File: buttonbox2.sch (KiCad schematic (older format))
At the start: 58 parts, among them J2 AVR-PDI-6, J4 Conn_01x03_Male, SW1 SW_SP3T, SW10 SW_Push, SW11 SW_Push, SW12 SW_Push, SW13 SW_Push, SW14 SW_Push, SW15 SW_Push, SW16 SW_Push, SW17 SW_Push, SW18 SW_Push, SW19 SW_Push, SW20 SW_Push, SW21 SW_Push, SW22 SW_Push, SW23 SW_Push, SW24 SW_Push, SW25 SW_Push, SW26 SW_Push, SW27 SW_Push, SW28 SW_Push, SW29 SW_Push, SW30 SW_Push, SW31 SW_Push, SW32 SW_Push, SW33 SW_Push, SW34 SW_Push, SW35 SW_Push, SW36 SW_Push, SW37 SW_Push, SW38 SW_Push, SW39 SW_Push, SW40 SW_Push, SW5 SW_Push, SW6 SW_Push, SW7 SW_Push, SW8 SW_Push, SW9 SW_Push, U1 ATxmega256A3-AU, U6 AMS1117-3.3, Y2 Crystal_GND24

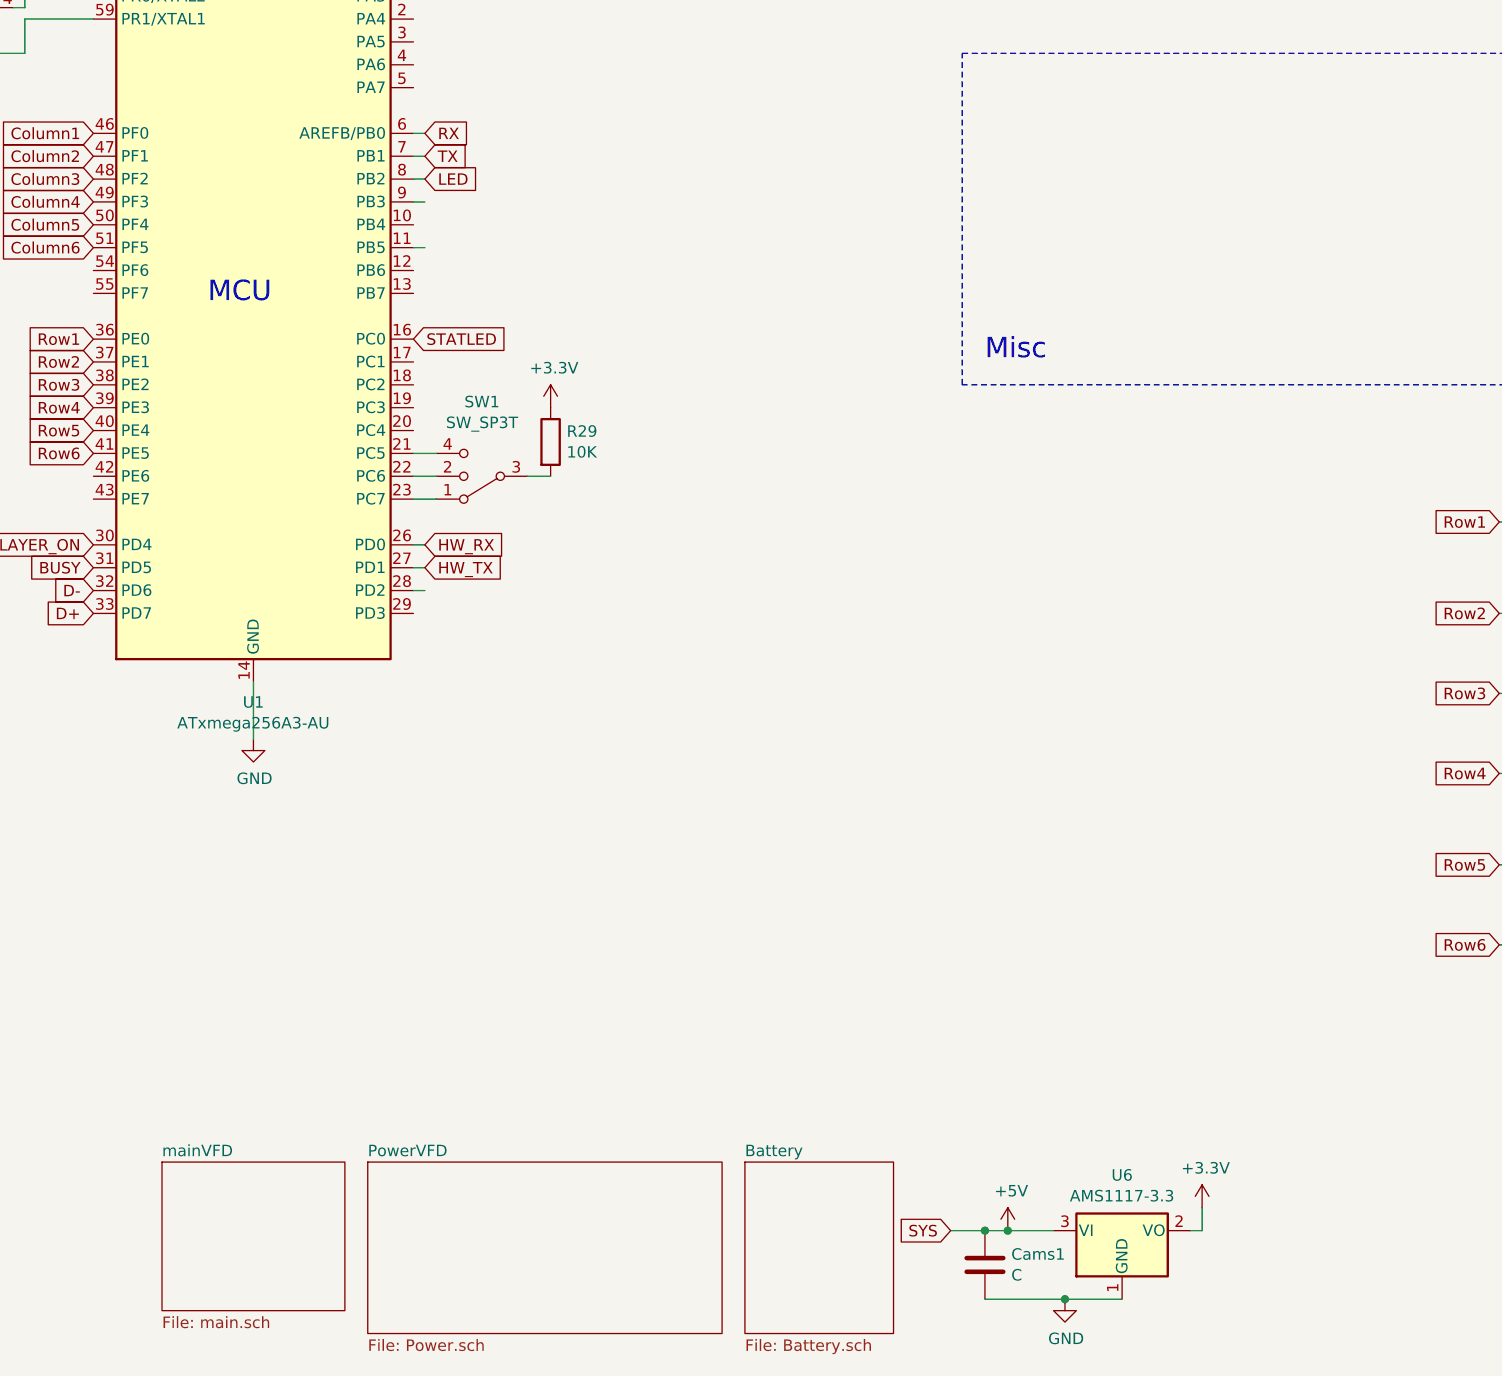
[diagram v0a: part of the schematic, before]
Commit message: Added hardware battery disconnect
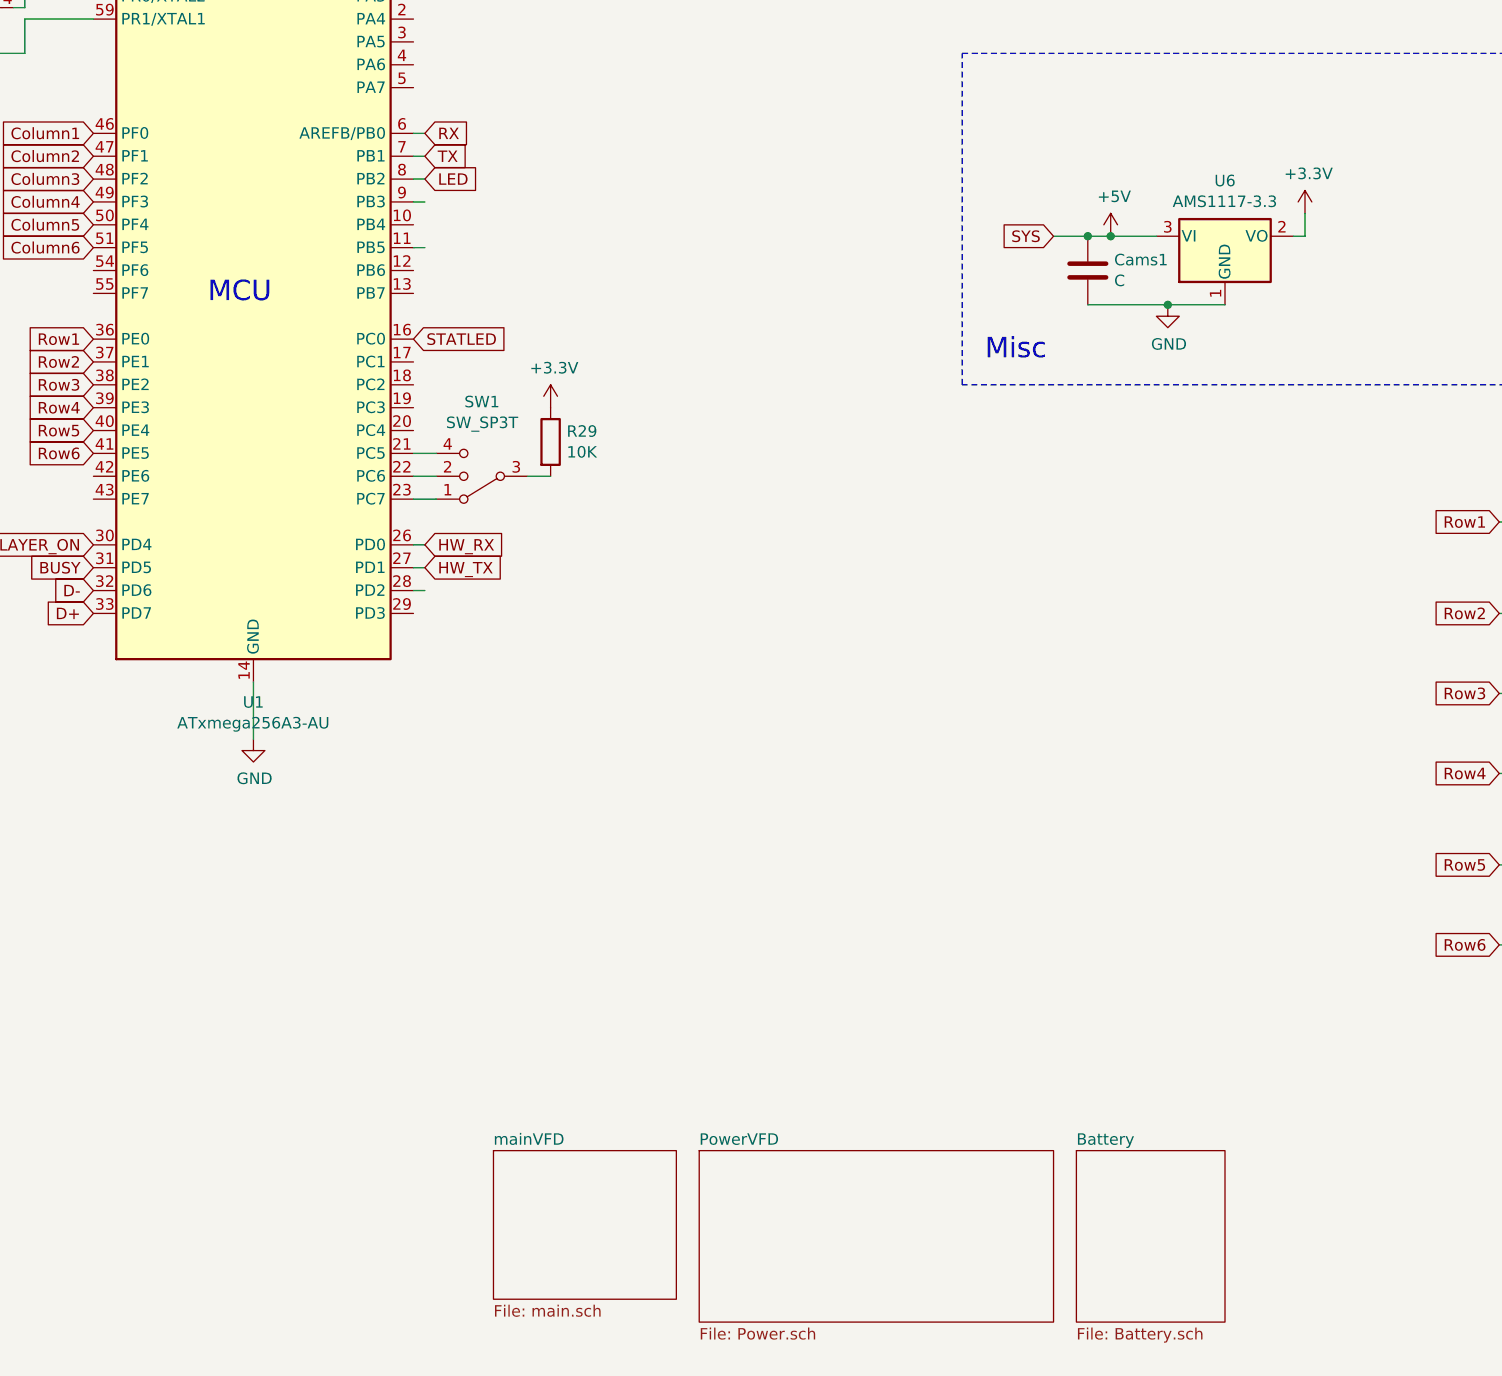
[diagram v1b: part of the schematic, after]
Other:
- moved on the sheet: Cams1, U6
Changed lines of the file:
@@
 L power:+3.3V #PWR0101
 U 1 1 617F15D4
-P 6750 7150
-F 0 "#PWR0101" H 6750 7000 50  0001 C CNN
-F 1 "+3.3V" H 6765 7323 50  0000 C CNN
-F 2 "" H 6750 7150 50  0001 C CNN
-F 3 "" H 6750 7150 50  0001 C CNN
-	1    6750 7150
+P 7200 2800
+F 0 "#PWR0101" H 7200 2650 50  0001 C CNN
+F 1 "+3.3V" H 7215 2973 50  0000 C CNN
+F 2 "" H 7200 2800 50  0001 C CNN
+F 3 "" H 7200 2800 50  0001 C CNN
+	1    7200 2800
 	1    0    0    -1
 $EndComp
@@
 $EndComp
 $Sheet
-S 4750 6950 650  750
+S 6200 6900 650  750
 U 60BEA0ED
 F0 "Battery" 50
@@
 L Regulator_Linear:AMS1117-3.3 U6
 U 1 1 60D07767
-P 6400 7250
-F 0 "U6" H 6400 7492 50  0000 C CNN
-F 1 "AMS1117-3.3" H 6400 7401 50  0000 C CNN
-F 2 "Package_TO_SOT_SMD:SOT-223-3_TabPin2" H 6400 7450 50  0001 C CNN
-F 3 "http://www.advanced-monolithic.com/pdf/ds1117.pdf" H 6500 7000 50  0001 C CNN
-	1    6400 7250
+P 6850 2900
+F 0 "U6" H 6850 3142 50  0000 C CNN
+F 1 "AMS1117-3.3" H 6850 3051 50  0000 C CNN
+F 2 "Package_TO_SOT_SMD:SOT-223-3_TabPin2" H 6850 3100 50  0001 C CNN
+F 3 "http://www.advanced-monolithic.com/pdf/ds1117.pdf" H 6950 2650 50  0001 C CNN
+	1    6850 2900
 	1    0    0    -1
 $EndComp
 Wire Wire Line
-	6700 7250 6750 7250
+	7150 2900 7200 2900
 Wire Wire Line
-	6750 7250 6750 7150
-Text GLabel 5650 7250 0    50   Input ~ 0
+	7200 2900 7200 2800
+Text GLabel 6100 2900 0    50   Input ~ 0
 SYS
 $Comp
 L power:GND #PWR0116
 U 1 1 60D21466
-P 6150 7550
-F 0 "#PWR0116" H 6150 7300 50  0001 C CNN
-F 1 "GND" H 6155 7377 50  0000 C CNN
-F 2 "" H 6150 7550 50  0001 C CNN
-F 3 "" H 6150 7550 50  0001 C CNN
-	1    6150 7550
+P 6600 3200
+F 0 "#PWR0116" H 6600 2950 50  0001 C CNN
+F 1 "GND" H 6605 3027 50  0000 C CNN
+F 2 "" H 6600 3200 50  0001 C CNN
+F 3 "" H 6600 3200 50  0001 C CNN
+	1    6600 3200
 	1    0    0    -1
 $EndComp
@@
 L Device:C Cams1
 U 1 1 60D3437E
-P 5800 7400
-F 0 "Cams1" H 5915 7446 50  0000 L CNN
-F 1 "C" H 5915 7355 50  0000 L CNN
-F 2 "Capacitor_SMD:C_0805_2012Metric" H 5838 7250 50  0001 C CNN
-F 3 "~" H 5800 7400 50  0001 C CNN
-	1    5800 7400
+P 6250 3050
+F 0 "Cams1" H 6365 3096 50  0000 L CNN
+F 1 "C" H 6365 3005 50  0000 L CNN
+F 2 "Capacitor_SMD:C_0805_2012Metric" H 6288 2900 50  0001 C CNN
+F 3 "~" H 6250 3050 50  0001 C CNN
+	1    6250 3050
 	1    0    0    -1
 $EndComp
 Wire Wire Line
-	6400 7550 6150 7550
-Connection ~ 6150 7550
-Connection ~ 5800 7250
+	6850 3200 6600 3200
+Connection ~ 6600 3200
+Connection ~ 6250 2900
 Wire Wire Line
-	5800 7250 5900 7250
+	6250 2900 6350 2900
 Wire Wire Line
-	5800 7550 6150 7550
+	6250 3200 6600 3200
 Wire Wire Line
-	5650 7250 5800 7250
+	6100 2900 6250 2900
 $Comp
 L power:+5V #PWR0117
 U 1 1 60D8DC4A
-P 5900 7250
-F 0 "#PWR0117" H 5900 7100 50  0001 C CNN
-F 1 "+5V" H 5915 7423 50  0000 C CNN
-F 2 "" H 5900 7250 50  0001 C CNN
-F 3 "" H 5900 7250 50  0001 C CNN
-	1    5900 7250
+P 6350 2900
+F 0 "#PWR0117" H 6350 2750 50  0001 C CNN
+F 1 "+5V" H 6365 3073 50  0000 C CNN
+F 2 "" H 6350 2900 50  0001 C CNN
+F 3 "" H 6350 2900 50  0001 C CNN
+	1    6350 2900
 	1    0    0    -1
 $EndComp
-Connection ~ 5900 7250
+Connection ~ 6350 2900
 Wire Wire Line
-	5900 7250 6100 7250
+	6350 2900 6550 2900
 $Sheet
-S 3100 6950 1550 750
+S 4550 6900 1550 750
 U 60E279E4
 F0 "PowerVFD" 50
@@
 $EndSheet
 $Sheet
-S 2200 6950 800  650
+S 3650 6900 800  650
 U 60E90241
 F0 "mainVFD" 50

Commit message: Ja crap toch weer aan de PCB gezeten
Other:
- moved on the sheet: Cams1, U6
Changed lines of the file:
@@
 Wire Notes Line
 	5700 2100 11100 2100
-Text Notes 5800 3450 0    89   ~ 0
+Text Notes 5750 3500 0    89   ~ 0
 Misc
 Wire Notes Line
@@
 L power:+3.3V #PWR0101
 U 1 1 617F15D4
-P 7200 2800
-F 0 "#PWR0101" H 7200 2650 50  0001 C CNN
-F 1 "+3.3V" H 7215 2973 50  0000 C CNN
-F 2 "" H 7200 2800 50  0001 C CNN
-F 3 "" H 7200 2800 50  0001 C CNN
-	1    7200 2800
+P 8200 2650
+F 0 "#PWR0101" H 8200 2500 50  0001 C CNN
+F 1 "+3.3V" H 8215 2823 50  0000 C CNN
+F 2 "" H 8200 2650 50  0001 C CNN
+F 3 "" H 8200 2650 50  0001 C CNN
+	1    8200 2650
 	1    0    0    -1
 $EndComp
@@
 $EndComp
 $Sheet
-S 6200 6900 650  750
+S 5500 6800 650  750
 U 60BEA0ED
 F0 "Battery" 50
@@
 L Regulator_Linear:AMS1117-3.3 U6
 U 1 1 60D07767
-P 6850 2900
-F 0 "U6" H 6850 3142 50  0000 C CNN
-F 1 "AMS1117-3.3" H 6850 3051 50  0000 C CNN
-F 2 "Package_TO_SOT_SMD:SOT-223-3_TabPin2" H 6850 3100 50  0001 C CNN
-F 3 "http://www.advanced-monolithic.com/pdf/ds1117.pdf" H 6950 2650 50  0001 C CNN
-	1    6850 2900
-	1    0    0    -1
-$EndComp
-Wire Wire Line
-	7150 2900 7200 2900
-Wire Wire Line
-	7200 2900 7200 2800
-Text GLabel 6100 2900 0    50   Input ~ 0
+P 7850 2750
+F 0 "U6" H 7850 2992 50  0000 C CNN
+F 1 "AMS1117-3.3" H 7850 2901 50  0000 C CNN
+F 2 "Package_TO_SOT_SMD:SOT-223-3_TabPin2" H 7850 2950 50  0001 C CNN
+F 3 "http://www.advanced-monolithic.com/pdf/ds1117.pdf" H 7950 2500 50  0001 C CNN
+	1    7850 2750
+	1    0    0    -1
+$EndComp
+Wire Wire Line
+	8150 2750 8200 2750
+Wire Wire Line
+	8200 2750 8200 2650
+Text GLabel 7100 2750 0    50   Input ~ 0
 SYS
 $Comp
 L power:GND #PWR0116
 U 1 1 60D21466
-P 6600 3200
-F 0 "#PWR0116" H 6600 2950 50  0001 C CNN
-F 1 "GND" H 6605 3027 50  0000 C CNN
-F 2 "" H 6600 3200 50  0001 C CNN
-F 3 "" H 6600 3200 50  0001 C CNN
-	1    6600 3200
+P 7600 3050
+F 0 "#PWR0116" H 7600 2800 50  0001 C CNN
+F 1 "GND" H 7605 2877 50  0000 C CNN
+F 2 "" H 7600 3050 50  0001 C CNN
+F 3 "" H 7600 3050 50  0001 C CNN
+	1    7600 3050
 	1    0    0    -1
 $EndComp
@@
 L Device:C Cams1
 U 1 1 60D3437E
-P 6250 3050
-F 0 "Cams1" H 6365 3096 50  0000 L CNN
-F 1 "C" H 6365 3005 50  0000 L CNN
-F 2 "Capacitor_SMD:C_0805_2012Metric" H 6288 2900 50  0001 C CNN
-F 3 "~" H 6250 3050 50  0001 C CNN
-	1    6250 3050
-	1    0    0    -1
-$EndComp
-Wire Wire Line
-	6850 3200 6600 3200
-Connection ~ 6600 3200
-Connection ~ 6250 2900
-Wire Wire Line
-	6250 2900 6350 2900
-Wire Wire Line
-	6250 3200 6600 3200
-Wire Wire Line
-	6100 2900 6250 2900
+P 7250 2900
+F 0 "Cams1" H 7365 2946 50  0000 L CNN
+F 1 "C" H 7365 2855 50  0000 L CNN
+F 2 "Capacitor_SMD:C_0805_2012Metric" H 7288 2750 50  0001 C CNN
+F 3 "~" H 7250 2900 50  0001 C CNN
+	1    7250 2900
+	1    0    0    -1
+$EndComp
+Wire Wire Line
+	7850 3050 7600 3050
+Connection ~ 7600 3050
+Connection ~ 7250 2750
+Wire Wire Line
+	7250 2750 7350 2750
+Wire Wire Line
+	7250 3050 7600 3050
+Wire Wire Line
+	7100 2750 7250 2750
 $Comp
 L power:+5V #PWR0117
 U 1 1 60D8DC4A
-P 6350 2900
-F 0 "#PWR0117" H 6350 2750 50  0001 C CNN
-F 1 "+5V" H 6365 3073 50  0000 C CNN
-F 2 "" H 6350 2900 50  0001 C CNN
-F 3 "" H 6350 2900 50  0001 C CNN
-	1    6350 2900
-	1    0    0    -1
-$EndComp
-Connection ~ 6350 2900
-Wire Wire Line
-	6350 2900 6550 2900
+P 7350 2750
+F 0 "#PWR0117" H 7350 2600 50  0001 C CNN
+F 1 "+5V" H 7365 2923 50  0000 C CNN
+F 2 "" H 7350 2750 50  0001 C CNN
+F 3 "" H 7350 2750 50  0001 C CNN
+	1    7350 2750
+	1    0    0    -1
+$EndComp
+Connection ~ 7350 2750
+Wire Wire Line
+	7350 2750 7550 2750
 $Sheet
-S 4550 6900 1550 750
+S 1400 6900 1550 750
 U 60E279E4
 F0 "PowerVFD" 50
@@
 $EndSheet
 $Sheet
-S 3650 6900 800  650
+S 500  6900 800  650
 U 60E90241
 F0 "mainVFD" 50

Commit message: Changed oscillator capacitor values from 22pF to 10pF
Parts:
- C5, C6: value 22p -> 10p
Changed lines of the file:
@@
 P 950 1700
 F 0 "C6" V 698 1700 50  0000 C CNN
-F 1 "22p" V 789 1700 50  0000 C CNN
+F 1 "10p" V 789 1700 50  0000 C CNN
 F 2 "Capacitor_SMD:C_0805_2012Metric" H 988 1550 50  0001 C CNN
 F 3 "~" H 950 1700 50  0001 C CNN
@@
 P 950 2100
 F 0 "C5" V 698 2100 50  0000 C CNN
-F 1 "22p" V 789 2100 50  0000 C CNN
+F 1 "10p" V 789 2100 50  0000 C CNN
 F 2 "Capacitor_SMD:C_0805_2012Metric" H 988 1950 50  0001 C CNN
 F 3 "~" H 950 2100 50  0001 C CNN

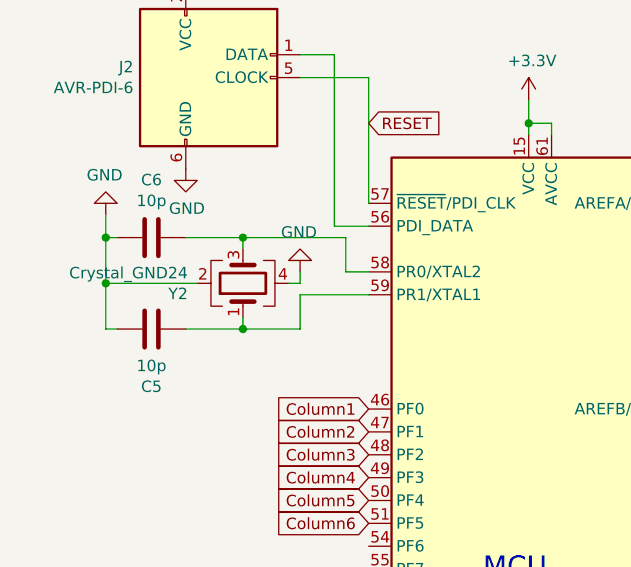
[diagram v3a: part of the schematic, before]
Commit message: Added SY6926 component values and some minor cleanup
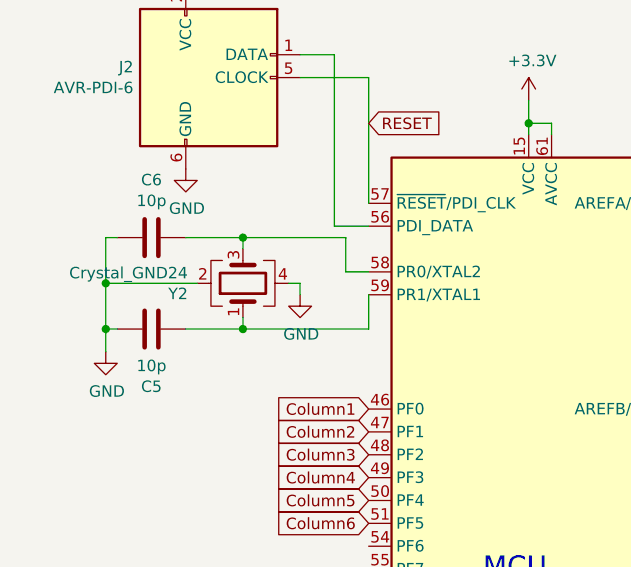
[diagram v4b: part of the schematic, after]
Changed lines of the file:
@@
 	2600 5100 2600 4850
 Wire Wire Line
-	1600 2100 1350 2100
-Wire Wire Line
-	1600 2100 1600 1950
+	1900 1950 1900 2100
 $Comp
 L power:GND #PWR019
 U 1 1 60046562
-P 1600 1850
-F 0 "#PWR019" H 1600 1600 50  0001 C CNN
-F 1 "GND" H 1605 1677 50  0000 C CNN
-F 2 "" H 1600 1850 50  0001 C CNN
-F 3 "" H 1600 1850 50  0001 C CNN
-	1    1600 1850
-	-1   0    0    1
-$EndComp
-Wire Wire Line
-	1600 1900 1600 1850
-Wire Wire Line
-	1550 1900 1600 1900
+P 1600 1950
+F 0 "#PWR019" H 1600 1700 50  0001 C CNN
+F 1 "GND" H 1605 1777 50  0000 C CNN
+F 2 "" H 1600 1950 50  0001 C CNN
+F 3 "" H 1600 1950 50  0001 C CNN
+	1    1600 1950
+	1    0    0    -1
+$EndComp
+Wire Wire Line
+	1600 1900 1600 1950
+Wire Wire Line
+	1600 1900 1550 1900
 Wire Wire Line
 	1800 1700 1350 1700
@@
 L power:GND #PWR05
 U 1 1 5FD12CA3
-P 750 1600
-F 0 "#PWR05" H 750 1350 50  0001 C CNN
-F 1 "GND" H 755 1427 50  0000 C CNN
-F 2 "" H 750 1600 50  0001 C CNN
-F 3 "" H 750 1600 50  0001 C CNN
-	1    750  1600
-	-1   0    0    1
+P 750 2200
+F 0 "#PWR05" H 750 1950 50  0001 C CNN
+F 1 "GND" H 755 2027 50  0000 C CNN
+F 2 "" H 750 2200 50  0001 C CNN
+F 3 "" H 750 2200 50  0001 C CNN
+	1    750  2200
+	1    0    0    -1
 $EndComp
 Connection ~ 1350 2100
@@
 	1100 1700 1350 1700
 Wire Wire Line
-	750  1700 750  1600
-Connection ~ 750  1700
+	750  2100 750  2200
 Wire Wire Line
 	800  1700 750  1700
@@
 Wire Wire Line
 	1900 1850 1800 1850
-Wire Wire Line
-	1600 1950 1900 1950
 $Comp
 L Connector:AVR-PDI-6 J2
@@
 Text GLabel 1900 4550 0    50   Input ~ 0
 D+
+Wire Wire Line
+	1350 2100 1900 2100
+Connection ~ 750  2100
 $EndSCHEMATC
